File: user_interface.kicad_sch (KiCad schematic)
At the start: 74 parts, among them J10 5V, J4 DVR FOUT, J5 3.3V, J6 DRV BOUT, J7 UART, J8 I2C, J9 5way Tracing, Q3 MMBT2222A, Q4 MMBT2222A, Q5 AO3401A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

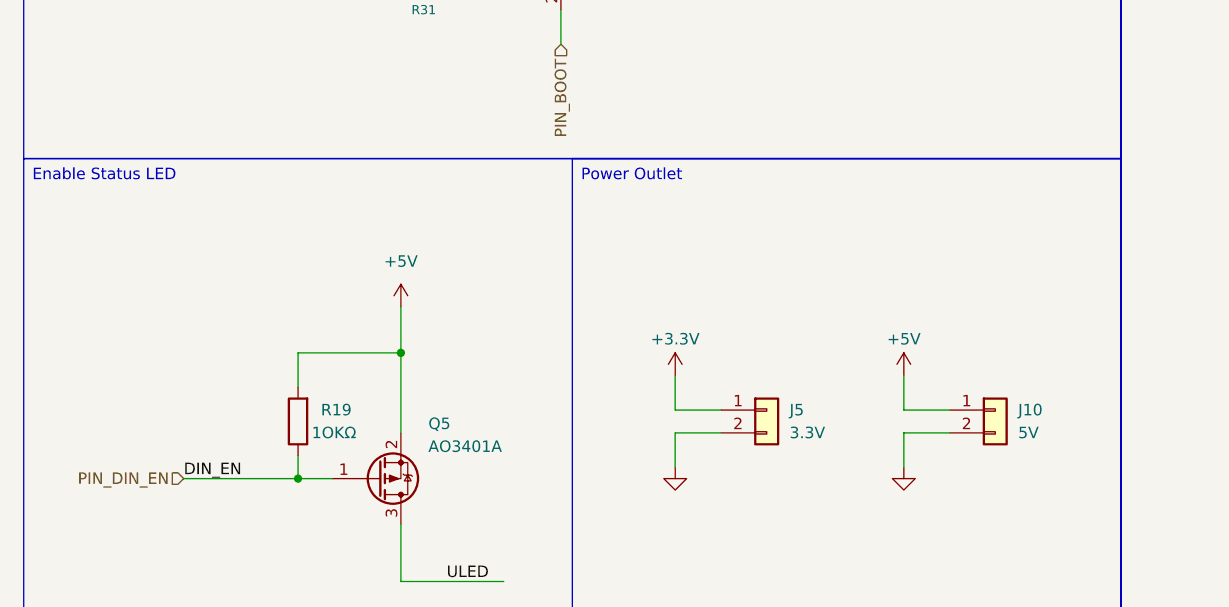
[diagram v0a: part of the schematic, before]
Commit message: Refine PCB layout: shift status LED for better visibility
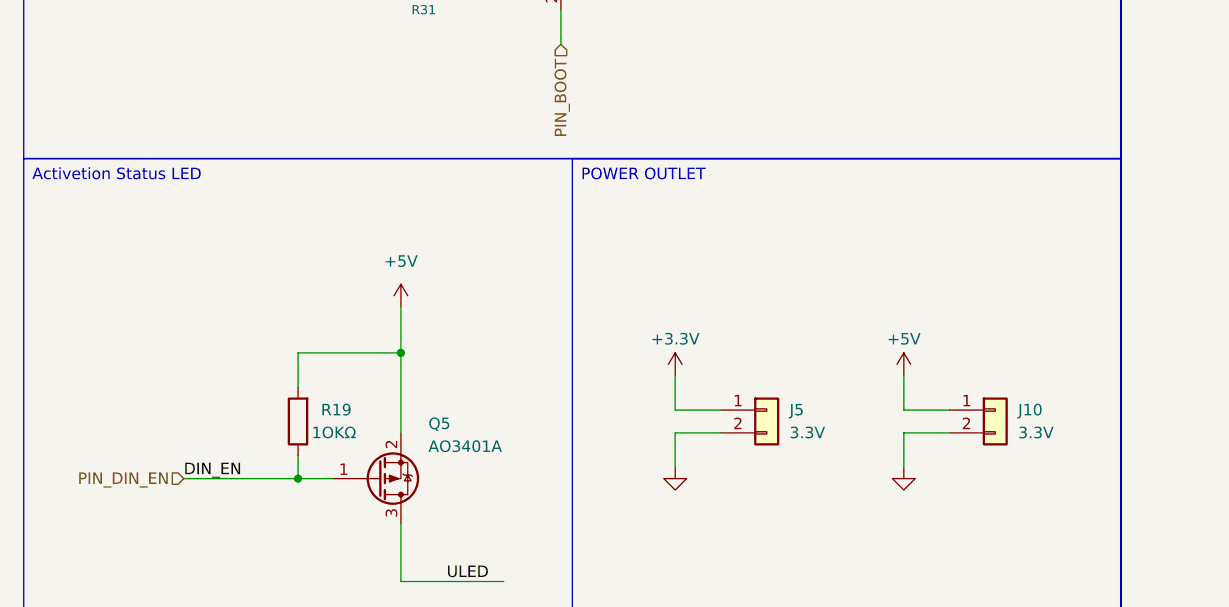
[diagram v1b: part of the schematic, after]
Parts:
- J10: value 5V -> 3.3V; footprint Connector_PinHeader_2.54mm:PinHeader_1x20_P2.54mm_Horizontal -> (none)
- J5: footprint Connector_PinHeader_2.54mm:PinHeader_1x20_P2.54mm_Horizontal -> (none)
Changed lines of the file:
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@@
 		)
 	)
-	(text_box "Enable Status LED"
+	(text_box "Activetion Status LED"
 		(exclude_from_sim no)
 		(at 17.78 144.78 0)
@@
 		)
 	)
-	(text_box "Power Outlet"
+	(text_box "POWER OUTLET"
 		(exclude_from_sim no)
 		(at 78.74 144.78 0)
@@
 			)
 		)
-		(property "Value" "5V"
+		(property "Value" "3.3V"
 			(at 128.27 175.2599 0)
 			(show_name no)
@@
 			)
 		)
-		(property "Footprint" "Connector_PinHeader_2.54mm:PinHeader_1x20_P2.54mm_Horizontal"
+		(property "Footprint" ""
 			(at 125.73 172.72 0)
 			(hide yes)
@@
 			)
 		)
-		(property "Footprint" "Connector_PinHeader_2.54mm:PinHeader_1x20_P2.54mm_Horizontal"
+		(property "Footprint" ""
 			(at 100.33 172.72 0)
 			(hide yes)
